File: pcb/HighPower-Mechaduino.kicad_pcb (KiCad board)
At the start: 2 copper layers, 60 x 60 mm, 133 parts, among them J1 SUPPLY, J2 STEPPER, P1 SWD, P2 USB, P3 PoStep25-32, P4 CONN_01X04, Q1 SSM3J328R, Q10 IPD079N06L3G, Q11 BSS138, Q2 BSS138, Q3 IPD079N06L3G, Q4 IPD079N06L3G, Q5 IPD079N06L3G, Q6 IPD079N06L3G, Q7 IPD079N06L3G, Q8 IPD079N06L3G, Q9 IPD079N06L3G, SW1 B3U-1000P, U1 AS5047D, U2 AP2112K-3.3TRG1, U3 AT24CS64-SSHM, U4 SAMD21G18A-A, U5 A4955GLPTR-T, U6 A4955GLPTR-T, U7 USBLC6-2SC6, U8 MCP16331T, U9 LM75BD, Y1 G83270022

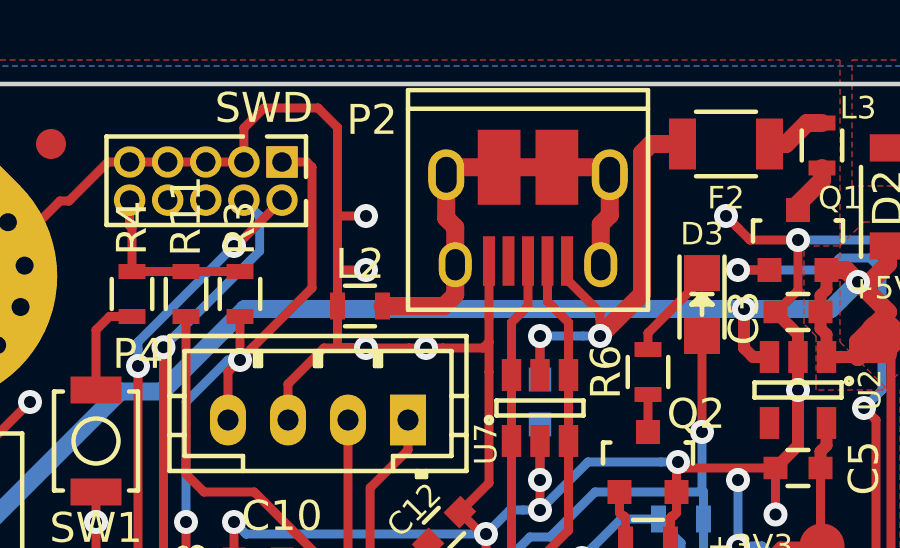
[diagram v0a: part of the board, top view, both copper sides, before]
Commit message: Add Text to pcb
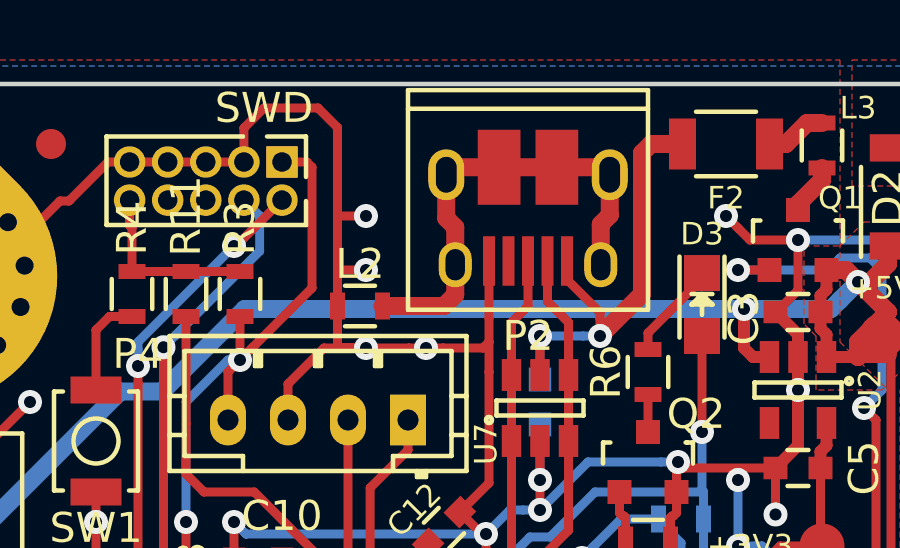
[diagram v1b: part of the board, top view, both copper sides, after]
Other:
- board text added: "HighPower-Mechaduino v0.1 designed by Thomas Pointhuber"
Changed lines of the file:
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@@
     (area 119.924999 69.924999 180.075001 130.075001)
     (thickness 1.6)
-    (drawings 25)
+    (drawings 26)
     (tracks 1563)
     (zones 0)
@@
     (tags "USB USB_B USB_micro USB_OTG")
     (attr smd)
-    (fp_text reference P2 (at 5.2 3.2 180) (layer F.SilkS)
+    (fp_text reference P2 (at 0 -4 180) (layer F.SilkS)
       (effects (font (size 1 1) (thickness 0.15)))
     )
@@
     )
   )
+  (gr_text "HighPower-Mechaduino v0.1\ndesigned by Thomas Pointhuber" (at 150 127.6) (layer B.SilkS)
+    (effects (font (size 0.9 0.9) (thickness 0.2)) (justify mirror))
+  )
   (gr_circle (center 160.2 74.8) (end 163.6 76.4) (layer Cmts.User) (width 0.12))

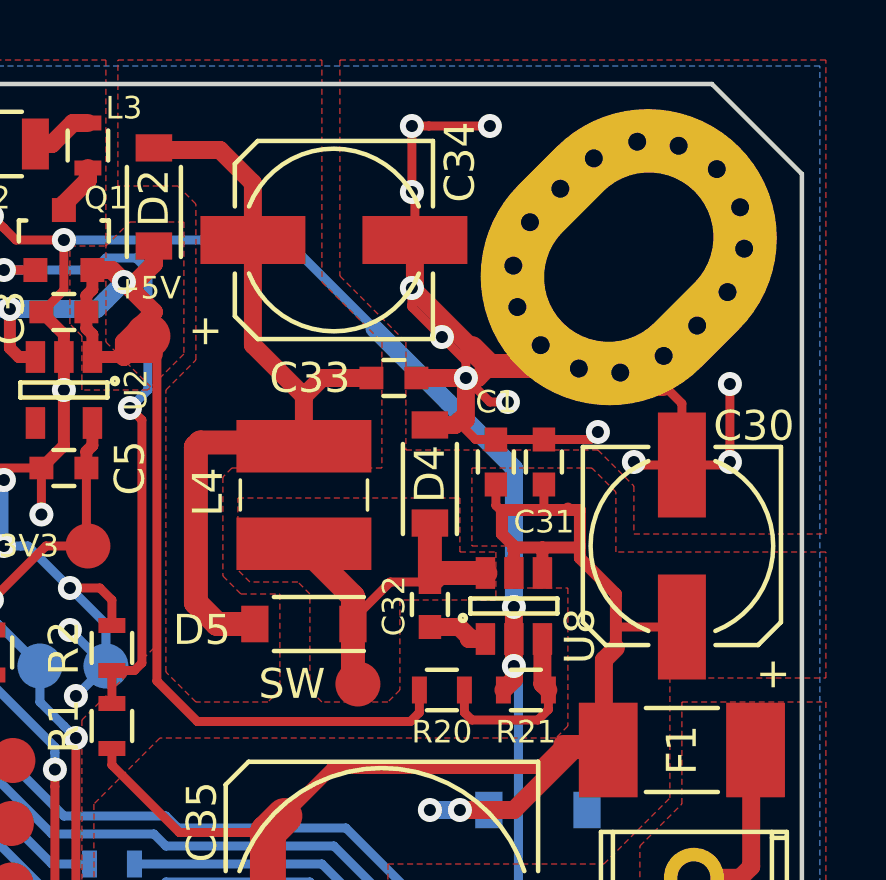
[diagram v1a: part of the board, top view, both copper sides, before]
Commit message: Update Capacitors
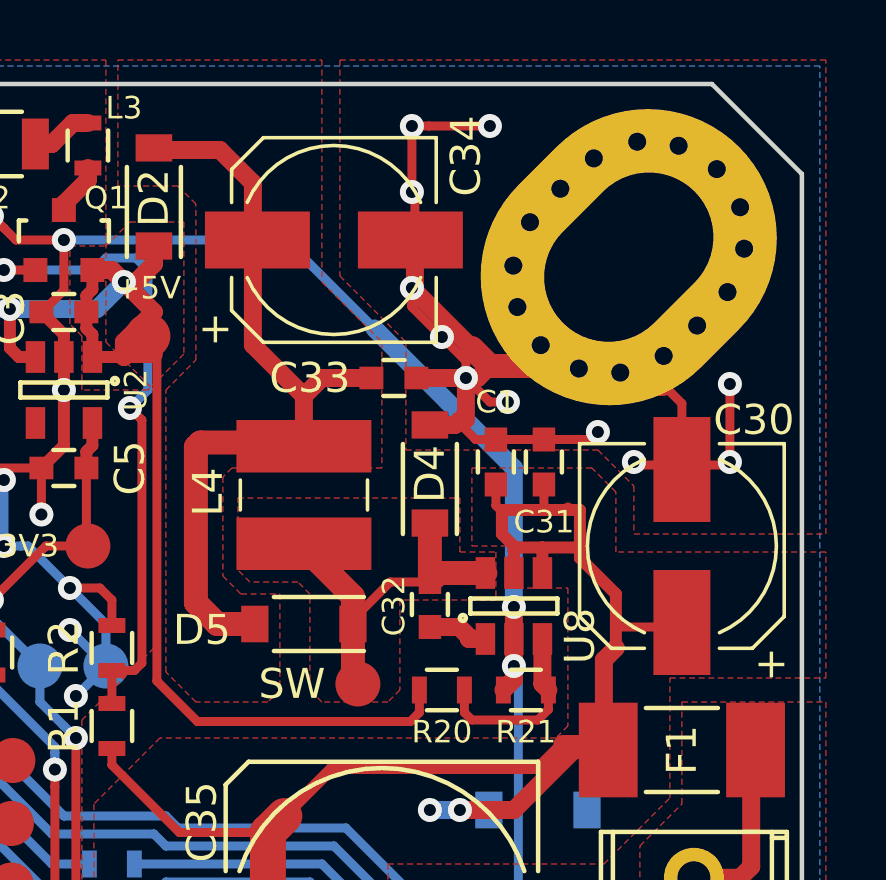
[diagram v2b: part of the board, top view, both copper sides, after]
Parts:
- C30, C34: footprint Capacitors_SMD:c_elec_6.3x5.8 -> Capacitors_SMD_local:c_elec_6.6x5.8

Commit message: Some little improvements
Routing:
- net Net-(R11-Pad2): track 13.2 -> 14.0 mm
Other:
- board text added: "GND"
- board text added: "VIN"

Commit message: Fix #5
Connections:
- P1 pad 6: Net-(P1-Pad6) -> (no net)
- P1 pad 8: Net-(P1-Pad8) -> (no net)
- P2 pad 4: /Protected_USB_Supply/ID -> (no net)
- U1 pad 10: Net-(U1-Pad10) -> (no net)
- U1 pad 14: Net-(U1-Pad14) -> (no net)
- U1 pad 6: Net-(U1-Pad6) -> (no net)
- U1 pad 7: Net-(U1-Pad7) -> (no net)
- U1 pad 8: Net-(U1-Pad8) -> (no net)
- U1 pad 9: Net-(U1-Pad9) -> (no net)
- U4 pad 14: /Arduino_Zero_Base/Arduino_D3 -> (no net)
- U4 pad 15: /Arduino_Zero_Base/Arduino_D1 -> (no net)
- U4 pad 16: /Arduino_Zero_Base/Arduino_D0 -> (no net)
- U4 pad 22: Net-(U4-Pad22) -> (no net)
- U4 pad 39: /Arduino_Zero_Base/Arduino_TX_LED -> (no net)
- U4 pad 41: /Arduino_Zero_Base/Arduino_USB_HOST_ENABLED -> (no net)
- U4 pad 48: /Arduino_Zero_Base/Arduino_RX_LED -> (no net)
- U5 pad 9: /PWM_Bridge_A4955-A/SLEEPn -> (no net)
- U6 pad 9: /PWM_Bridge_A4955-B/SLEEPn -> (no net)
- U9 pad 3: Net-(U9-Pad3) -> (no net)
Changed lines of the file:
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@@
     (zones 0)
     (modules 133)
-    (nets 100)
+    (nets 81)
   )
   (page A4)
@@
   (net 79 /MCP16331_5V/Vfb)
   (net 80 "Net-(C33-Pad1)")
-  (net 81 "Net-(P1-Pad6)")
-  (net 82 "Net-(P1-Pad8)")
-  (net 83 "Net-(U1-Pad6)")
-  (net 84 "Net-(U1-Pad7)")
-  (net 85 "Net-(U1-Pad8)")
-  (net 86 "Net-(U1-Pad9)")
-  (net 87 "Net-(U1-Pad10)")
-  (net 88 "Net-(U1-Pad14)")
-  (net 89 "Net-(U9-Pad3)")
-  (net 90 /Arduino_Zero_Base/Arduino_D1)
-  (net 91 /Arduino_Zero_Base/Arduino_D0)
-  (net 92 "Net-(U4-Pad22)")
-  (net 93 /Arduino_Zero_Base/Arduino_TX_LED)
-  (net 94 /Arduino_Zero_Base/Arduino_USB_HOST_ENABLED)
-  (net 95 /Arduino_Zero_Base/Arduino_RX_LED)
-  (net 96 /Protected_USB_Supply/ID)
-  (net 97 /Arduino_Zero_Base/Arduino_D3)
-  (net 98 /PWM_Bridge_A4955-A/SLEEPn)
-  (net 99 /PWM_Bridge_A4955-B/SLEEPn)
   (net_class Default "Dies ist die voreingestellte Netzklasse."
     (clearance 0.15)
@@
     (add_net /A_IN)
     (add_net /Arduino_Zero_Base/Arduino_AREF)
-    (add_net /Arduino_Zero_Base/Arduino_D0)
-    (add_net /Arduino_Zero_Base/Arduino_D1)
-    (add_net /Arduino_Zero_Base/Arduino_D3)
     (add_net /Arduino_Zero_Base/Arduino_RXD)
-    (add_net /Arduino_Zero_Base/Arduino_RX_LED)
     (add_net /Arduino_Zero_Base/Arduino_TXD)
-    (add_net /Arduino_Zero_Base/Arduino_TX_LED)
-    (add_net /Arduino_Zero_Base/Arduino_USB_HOST_ENABLED)
     (add_net /IN1)
     (add_net /IN2)
@@
     (add_net /OCLn1)
     (add_net /OCLn2)
-    (add_net /PWM_Bridge_A4955-A/SLEEPn)
     (add_net /PWM_Bridge_A4955-A/VREF)
-    (add_net /PWM_Bridge_A4955-B/SLEEPn)
     (add_net /PWM_Bridge_A4955-B/VREF)
-    (add_net /Protected_USB_Supply/ID)
     (add_net /Protected_USB_Supply/VBUS)
     (add_net /RESET)
@@
     (add_net "Net-(F2-Pad1)")
     (add_net "Net-(L2-Pad1)")
-    (add_net "Net-(P1-Pad6)")
-    (add_net "Net-(P1-Pad8)")
     (add_net "Net-(P3-Pad7)")
     (add_net "Net-(Q1-Pad1)")
@@
     (add_net "Net-(R18-Pad1)")
     (add_net "Net-(R4-Pad1)")
-    (add_net "Net-(U1-Pad10)")
-    (add_net "Net-(U1-Pad14)")
-    (add_net "Net-(U1-Pad6)")
-    (add_net "Net-(U1-Pad7)")
-    (add_net "Net-(U1-Pad8)")
-    (add_net "Net-(U1-Pad9)")
-    (add_net "Net-(U4-Pad22)")
-    (add_net "Net-(U9-Pad3)")
     (add_net VDD)
   )
@@
     (tags "resistor 0603")
     (attr smd)
-    (fp_text reference R11 (at -1.8 0 360) (layer F.SilkS)
+    (fp_text reference R11 (at -1.8 0) (layer F.SilkS)
       (effects (font (size 0.75 0.75) (thickness 0.15)))
     )
@@
     (pad 4 smd rect (at -2.7 1.905 180) (size 1.55 0.6) (layers F.Cu F.Paste F.Mask)
       (net 1 GND))
-    (pad 3 smd rect (at -2.7 0.635 180) (size 1.55 0.6) (layers F.Cu F.Paste F.Mask)
-      (net 89 "Net-(U9-Pad3)"))
+    (pad 3 smd rect (at -2.7 0.635 180) (size 1.55 0.6) (layers F.Cu F.Paste F.Mask))
     (pad 2 smd rect (at -2.7 -0.635 180) (size 1.55 0.6) (layers F.Cu F.Paste F.Mask)
       (net 53 /SCL))
@@
     (pad 4 thru_hole circle (at 1.27 1.27 270) (size 1.05 1.05) (drill 0.65) (layers *.Cu *.Mask F.SilkS)
       (net 29 /SWCLK))
-    (pad 6 thru_hole circle (at 1.27 2.54 270) (size 1.05 1.05) (drill 0.65) (layers *.Cu *.Mask F.SilkS)
-      (net 81 "Net-(P1-Pad6)"))
-    (pad 8 thru_hole circle (at 1.27 3.81 270) (size 1.05 1.05) (drill 0.65) (layers *.Cu *.Mask F.SilkS)
-      (net 82 "Net-(P1-Pad8)"))
+    (pad 6 thru_hole circle (at 1.27 2.54 270) (size 1.05 1.05) (drill 0.65) (layers *.Cu *.Mask F.SilkS))
+    (pad 8 thru_hole circle (at 1.27 3.81 270) (size 1.05 1.05) (drill 0.65) (layers *.Cu *.Mask F.SilkS))
     (pad 10 thru_hole circle (at 1.27 5.08 270) (size 1.05 1.05) (drill 0.65) (layers *.Cu *.Mask F.SilkS)
       (net 30 /RESET))
@@
     (pad 3 smd rect (at -0.0009 -1.5 270) (size 1.65 0.4) (layers F.Cu F.Paste F.Mask)
       (net 33 /USB_D+))
-    (pad 4 smd rect (at 0.65 -1.5 270) (size 1.65 0.4) (layers F.Cu F.Paste F.Mask)
-      (net 96 /Protected_USB_Supply/ID))
+    (pad 4 smd rect (at 0.65 -1.5 270) (size 1.65 0.4) (layers F.Cu F.Paste F.Mask))
     (pad 5 smd rect (at 1.3 -1.5 270) (size 1.65 0.4) (layers F.Cu F.Paste F.Mask)
       (net 1 GND))
@@
     (pad 5 smd rect (at -2.95 -0.65 180) (size 1.45 0.45) (layers B.Cu B.Paste B.Mask)
       (net 1 GND))
-    (pad 6 smd rect (at -2.95 -1.3 180) (size 1.45 0.45) (layers B.Cu B.Paste B.Mask)
-      (net 83 "Net-(U1-Pad6)"))
-    (pad 7 smd rect (at -2.95 -1.95 180) (size 1.45 0.45) (layers B.Cu B.Paste B.Mask)
-      (net 84 "Net-(U1-Pad7)"))
-    (pad 8 smd rect (at 2.95 -1.95 180) (size 1.45 0.45) (layers B.Cu B.Paste B.Mask)
-      (net 85 "Net-(U1-Pad8)"))
-    (pad 9 smd rect (at 2.95 -1.3 180) (size 1.45 0.45) (layers B.Cu B.Paste B.Mask)
-      (net 86 "Net-(U1-Pad9)"))
-    (pad 10 smd rect (at 2.95 -0.65 180) (size 1.45 0.45) (layers B.Cu B.Paste B.Mask)
-      (net 87 "Net-(U1-Pad10)"))
+    (pad 6 smd rect (at -2.95 -1.3 180) (size 1.45 0.45) (layers B.Cu B.Paste B.Mask))
+    (pad 7 smd rect (at -2.95 -1.95 180) (size 1.45 0.45) (layers B.Cu B.Paste B.Mask))
+    (pad 8 smd rect (at 2.95 -1.95 180) (size 1.45 0.45) (layers B.Cu B.Paste B.Mask))
+    (pad 9 smd rect (at 2.95 -1.3 180) (size 1.45 0.45) (layers B.Cu B.Paste B.Mask))
+    (pad 10 smd rect (at 2.95 -0.65 180) (size 1.45 0.45) (layers B.Cu B.Paste B.Mask))
     (pad 11 smd rect (at 2.95 0 180) (size 1.45 0.45) (layers B.Cu B.Paste B.Mask)
       (net 5 "Net-(C4-Pad2)"))
@@
     (pad 13 smd rect (at 2.95 1.3 180) (size 1.45 0.45) (layers B.Cu B.Paste B.Mask)
       (net 1 GND))
-    (pad 14 smd rect (at 2.95 1.95 180) (size 1.45 0.45) (layers B.Cu B.Paste B.Mask)
-      (net 88 "Net-(U1-Pad14)"))
+    (pad 14 smd rect (at 2.95 1.95 180) (size 1.45 0.45) (layers B.Cu B.Paste B.Mask))
     (model Housings_SSOP.3dshapes/TSSOP-14_4.4x5mm_Pitch0.65mm.wrl
       (at (xyz 0 0 0))
@@
     (pad 13 smd rect (at -2.75 4.35 135) (size 1.3 0.25) (layers F.Cu F.Paste F.Mask)
       (net 50 /VREF2))
-    (pad 14 smd rect (at -2.25 4.35 135) (size 1.3 0.25) (layers F.Cu F.Paste F.Mask)
-      (net 97 /Arduino_Zero_Base/Arduino_D3))
-    (pad 15 smd rect (at -1.749999 4.35 135) (size 1.3 0.25) (layers F.Cu F.Paste F.Mask)
-      (net 90 /Arduino_Zero_Base/Arduino_D1))
-    (pad 16 smd rect (at -1.25 4.35 135) (size 1.3 0.25) (layers F.Cu F.Paste F.Mask)
-      (net 91 /Arduino_Zero_Base/Arduino_D0))
+    (pad 14 smd rect (at -2.25 4.35 135) (size 1.3 0.25) (layers F.Cu F.Paste F.Mask))
+    (pad 15 smd rect (at -1.749999 4.35 135) (size 1.3 0.25) (layers F.Cu F.Paste F.Mask))
+    (pad 16 smd rect (at -1.25 4.35 135) (size 1.3 0.25) (layers F.Cu F.Paste F.Mask))
     (pad 17 smd rect (at -0.750001 4.35 135) (size 1.3 0.25) (layers F.Cu F.Paste F.Mask)
       (net 3 +3V3))
@@
     (pad 21 smd rect (at 1.25 4.35 135) (size 1.3 0.25) (layers F.Cu F.Paste F.Mask)
       (net 58 /SPI_MISO))
-    (pad 22 smd rect (at 1.749999 4.35 135) (size 1.3 0.25) (layers F.Cu F.Paste F.Mask)
-      (net 92 "Net-(U4-Pad22)"))
+    (pad 22 smd rect (at 1.749999 4.35 135) (size 1.3 0.25) (layers F.Cu F.Paste F.Mask))
     (pad 23 smd rect (at 2.25 4.35 135) (size 1.3 0.25) (layers F.Cu F.Paste F.Mask)
       (net 47 /STP_ERROR))
@@
     (pad 38 smd rect (at 2.25 -4.35 135) (size 1.3 0.25) (layers F.Cu F.Paste F.Mask)
       (net 65 /Arduino_Zero_Base/Arduino_RXD))
-    (pad 39 smd rect (at 1.749999 -4.35 135) (size 1.3 0.25) (layers F.Cu F.Paste F.Mask)
-      (net 93 /Arduino_Zero_Base/Arduino_TX_LED))
+    (pad 39 smd rect (at 1.749999 -4.35 135) (size 1.3 0.25) (layers F.Cu F.Paste F.Mask))
     (pad 40 smd rect (at 1.25 -4.35 135) (size 1.3 0.25) (layers F.Cu F.Paste F.Mask)
       (net 51 "Net-(R11-Pad2)"))
-    (pad 41 smd rect (at 0.750001 -4.35 135) (size 1.3 0.25) (layers F.Cu F.Paste F.Mask)
-      (net 94 /Arduino_Zero_Base/Arduino_USB_HOST_ENABLED))
+    (pad 41 smd rect (at 0.750001 -4.35 135) (size 1.3 0.25) (layers F.Cu F.Paste F.Mask))
     (pad 42 smd rect (at 0.25 -4.35 135) (size 1.3 0.25) (layers F.Cu F.Paste F.Mask)
       (net 1 GND))
@@
     (pad 47 smd rect (at -2.25 -4.35 135) (size 1.3 0.25) (layers F.Cu F.Paste F.Mask)
       (net 78 /A_IN))
-    (pad 48 smd rect (at -2.75 -4.35 135) (size 1.3 0.25) (layers F.Cu F.Paste F.Mask)
-      (net 95 /Arduino_Zero_Base/Arduino_RX_LED))
+    (pad 48 smd rect (at -2.75 -4.35 135) (size 1.3 0.25) (layers F.Cu F.Paste F.Mask))
     (model Housings_QFP.3dshapes/TQFP-48_7x7mm_Pitch0.5mm.wrl
       (at (xyz 0 0 0))
@@
     (pad 10 smd rect (at -2.95 -2.925) (size 1.45 0.45) (layers B.Cu B.Paste B.Mask)
       (net 38 "Net-(Q4-Pad3)"))
-    (pad 9 smd rect (at -2.95 -2.275) (size 1.45 0.45) (layers B.Cu B.Paste B.Mask)
-      (net 98 /PWM_Bridge_A4955-A/SLEEPn))
+    (pad 9 smd rect (at -2.95 -2.275) (size 1.45 0.45) (layers B.Cu B.Paste B.Mask))
     (pad 8 smd rect (at -2.95 -1.625) (size 1.45 0.45) (layers B.Cu B.Paste B.Mask)
       (net 54 "Net-(R15-Pad1)"))
@@
     (pad 8 smd rect (at -2.95 -1.625 270) (size 1.45 0.45) (layers B.Cu B.Paste B.Mask)
       (net 55 "Net-(R18-Pad1)"))
-    (pad 9 smd rect (at -2.95 -2.275 270) (size 1.45 0.45) (layers B.Cu B.Paste B.Mask)
-      (net 99 /PWM_Bridge_A4955-B/SLEEPn))
+    (pad 9 smd rect (at -2.95 -2.275 270) (size 1.45 0.45) (layers B.Cu B.Paste B.Mask))
     (pad 10 smd rect (at -2.95 -2.925 270) (size 1.45 0.45) (layers B.Cu B.Paste B.Mask)
       (net 43 "Net-(Q10-Pad3)"))

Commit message: Fix #7
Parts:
- removed C2: 1µ, Capacitors_SMD:C_0603
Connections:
- C4 pad 2: Net-(C4-Pad2) -> +3V3
- U1 pad 11: Net-(C4-Pad2) -> +3V3
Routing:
- net GND: track 543.1 -> 540.3 mm
- net Net-(C4-Pad2): track 2.15 -> 0.00 mm

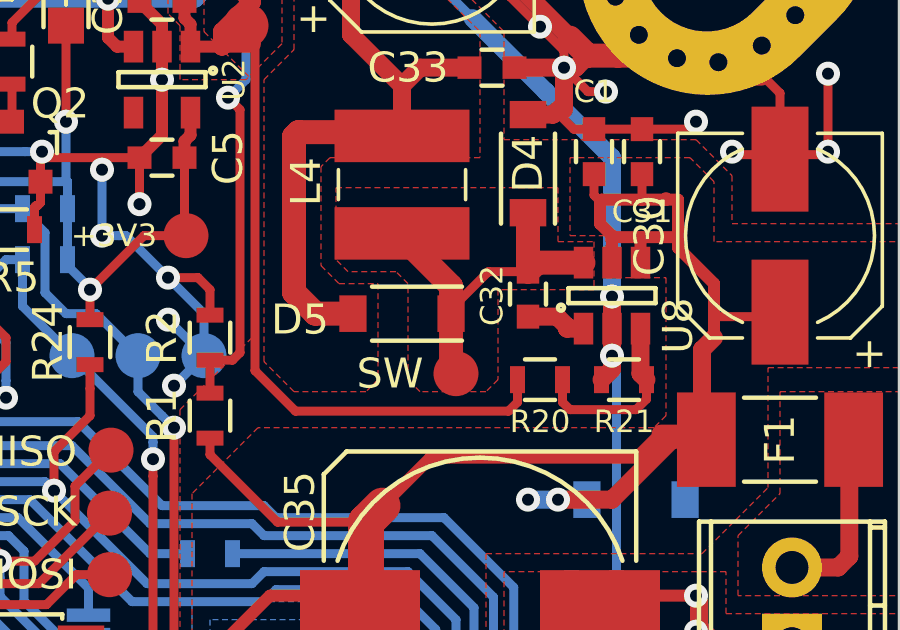
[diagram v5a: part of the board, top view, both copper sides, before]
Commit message: Fix schematic error described in #8
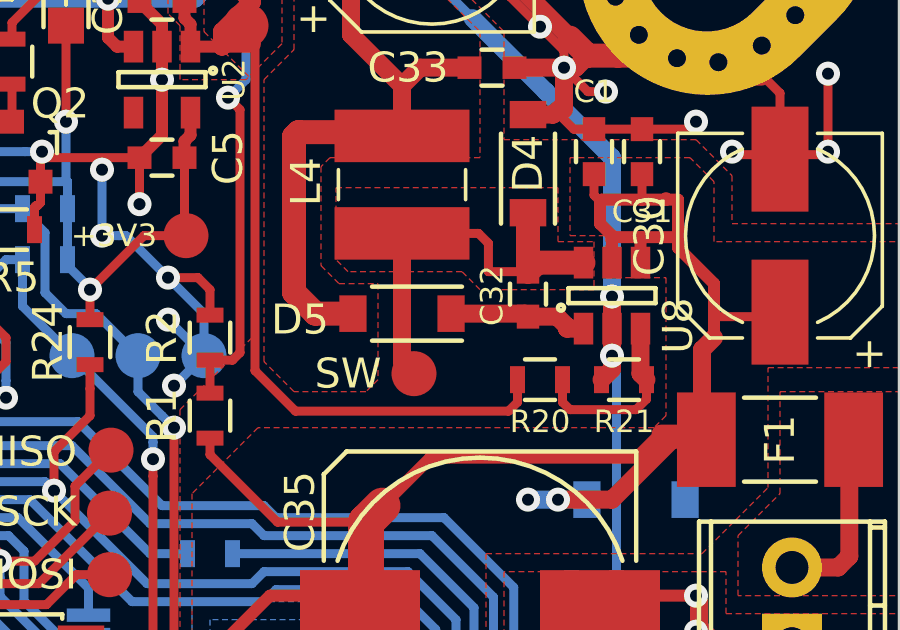
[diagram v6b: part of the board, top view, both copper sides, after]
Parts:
- moved W18 1.40 mm to (163.8, 90.0)
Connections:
- D5 pad 1: Net-(C32-Pad2) -> Net-(C32-Pad1)
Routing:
- net Net-(C32-Pad1): track 2.06 -> 4.82 mm
- net Net-(C32-Pad2): track 12.0 -> 14.1 mm
